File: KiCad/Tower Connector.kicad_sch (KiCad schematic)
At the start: 0 parts

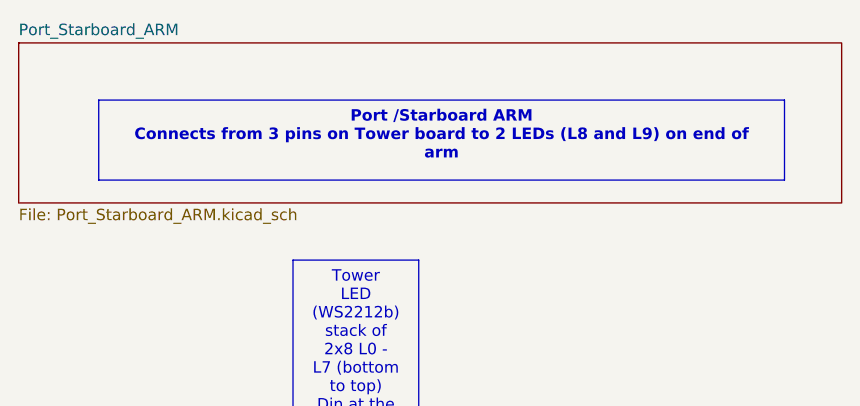
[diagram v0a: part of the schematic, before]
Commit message: Refactored to separate PS arm from tower connector
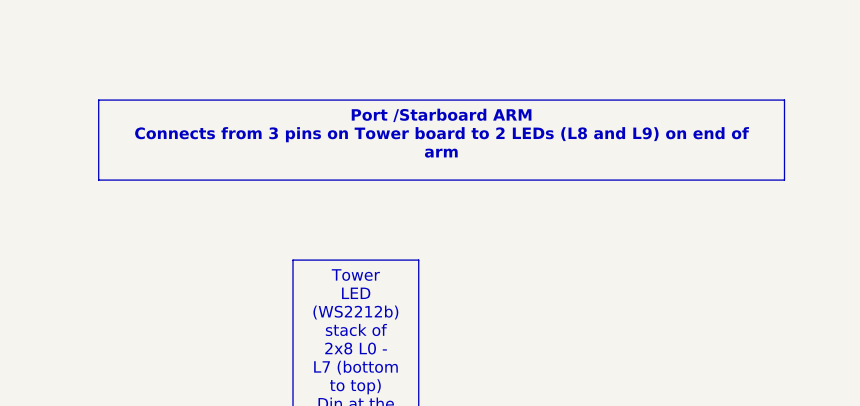
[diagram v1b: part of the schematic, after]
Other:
- removed sheet Port_Starboard_ARM
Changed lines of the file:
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@@
-		)
-	)
-	(sheet
-		(at 54.61 77.47)
-		(size 91.44 17.78)
-		(exclude_from_sim no)
-		(in_bom yes)
-		(on_board yes)
-		(dnp no)
-		(fields_autoplaced yes)
-		(stroke
-			(width 0.1524)
-			(type solid)
-		)
-		(fill
-			(color 0 0 0 0)
-		)
-		(property "Sheetname" "Port_Starboard_ARM"
-			(at 54.61 76.7584 0)
-			(show_name no)
-			(do_not_autoplace no)
-			(effects
-				(font
-					(size 1.27 1.27)
-				)
-				(justify left bottom)
-			)
-		)
-		(property "Sheetfile" "Port_Starboard_ARM.kicad_sch"
-			(at 54.61 95.8346 0)
-			(show_name no)
-			(do_not_autoplace no)
-			(effects
-				(font
-					(size 1.27 1.27)
-				)
-				(justify left top)
-			)
-		)
-		(instances
-			(project "Tower Connector and PS Arm"
-				(path "/ec70a6ff-e411-44e0-b8ff-0fb3c8ca2521"
-					(page "3")
-				)
-			)
 		)
 	)
